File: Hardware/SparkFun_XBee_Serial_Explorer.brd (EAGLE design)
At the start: 57.1 x 48.3 mm, 45 parts, among them Q1 MBT2222, U1 MAX232SOIC16, U2 XBEE-1B3, U3 LM117

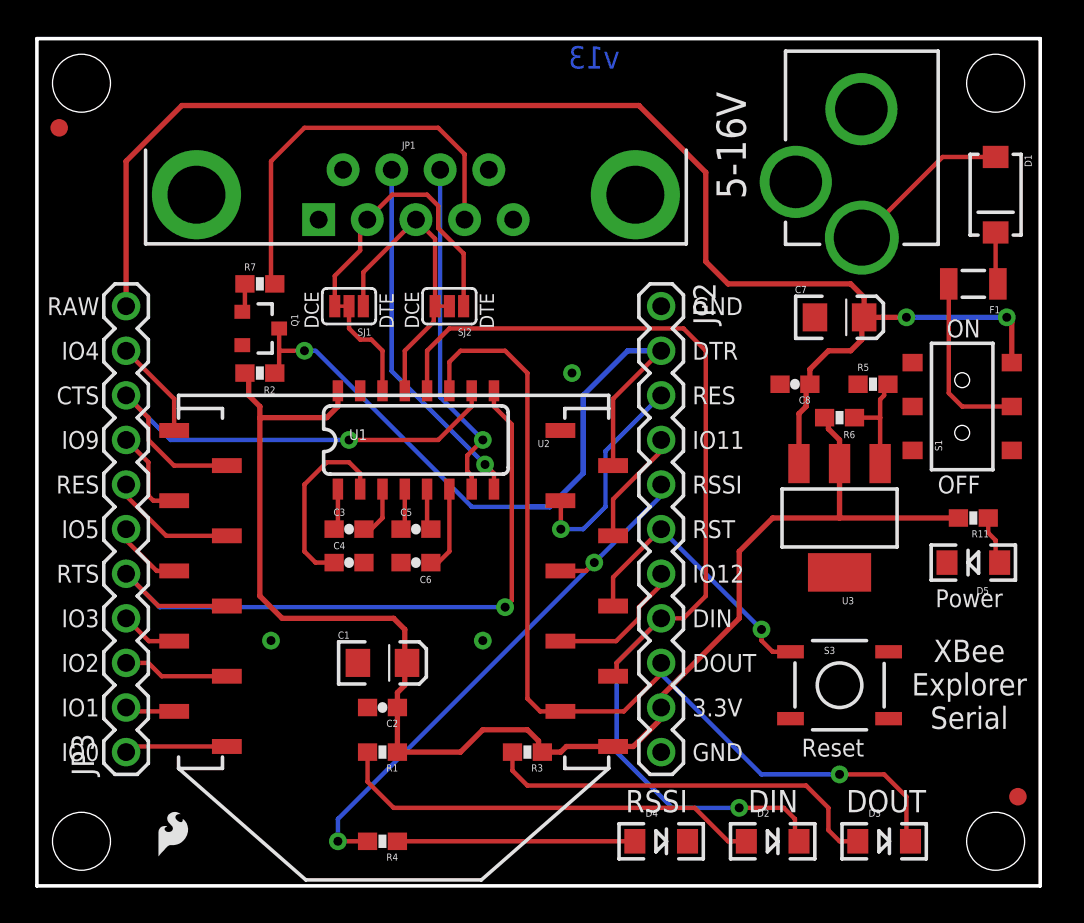
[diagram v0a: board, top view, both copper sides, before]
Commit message: Adding in test points for QC
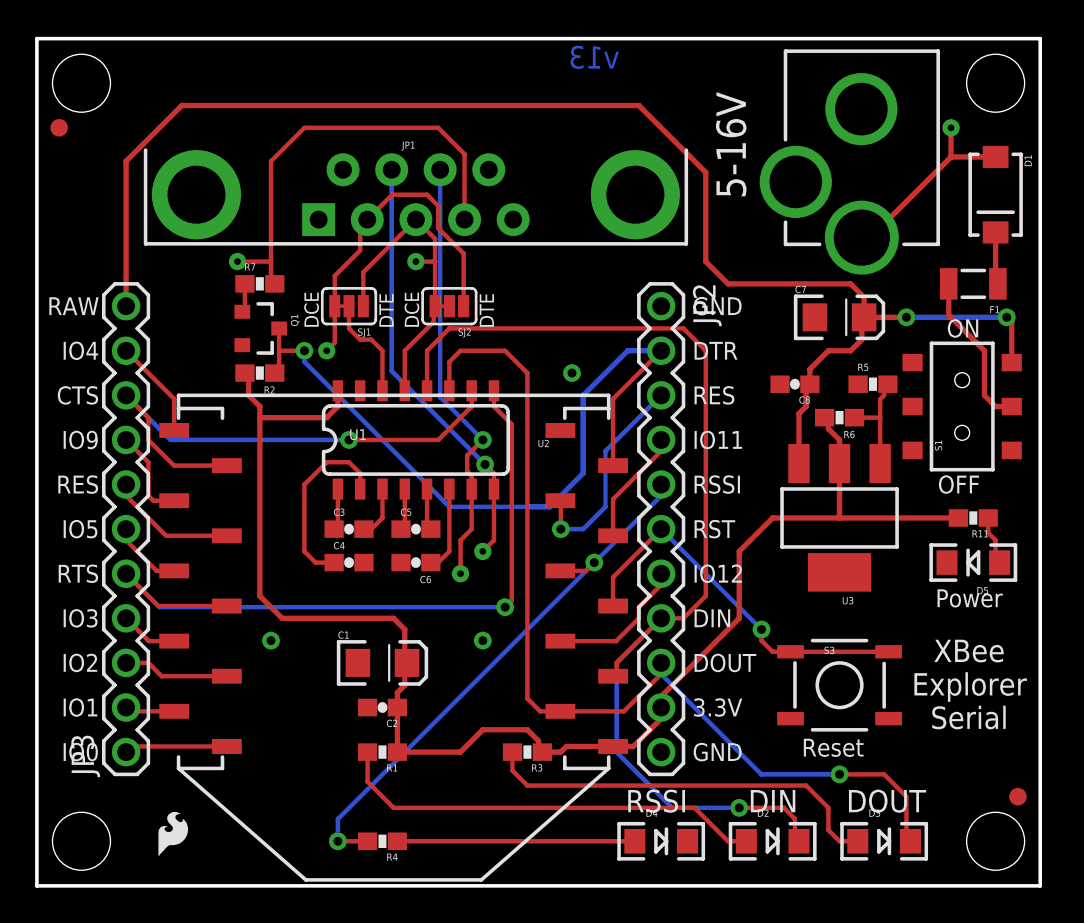
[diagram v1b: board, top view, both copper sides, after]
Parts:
- added TP1, TP2, TP3, TP4, TP5, TP6: TEST-POINTTP_15TH_THRU, SparkFun-Passives:TP_15TH
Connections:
- net N$15: now also TP6.P$1
- net RS232-CTS: now also TP2.P$1
- net RS232-DTR: now also TP3.P$1
- net RS232-RTS: now also TP1.P$1
- net RS232-RX: now also TP4.P$1
- net RS232-TX: now also TP5.P$1
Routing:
- net RESET: track 16.1 -> 22.1 mm
- net RS232-CTS: track 19.7 -> 24.8 mm
- net RS232-RTS: track 20.6 -> 24.4 mm
- net RS232-TX: track 16.9 -> 19.6 mm
- net RS232-DTR: track 23.2 -> 25.1 mm
- net N$15: track 9.52 -> 11.2 mm
- net N$11: track 10.1 -> 9.01 mm
- net RS232-RX: track 11.6 -> 12.6 mm
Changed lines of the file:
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@@
 <layer number="47" name="Measures" color="7" fill="1" visible="no" active="yes"/>
 <layer number="48" name="Document" color="7" fill="1" visible="no" active="yes"/>
-<layer number="49" name="Reference" color="7" fill="1" visible="no" active="yes"/>
+<layer number="49" name="Reference" color="7" fill="1" visible="yes" active="yes"/>
 <layer number="50" name="dxf" color="7" fill="1" visible="no" active="yes"/>
 <layer number="51" name="tDocu" color="6" fill="1" visible="yes" active="yes"/>
@@
 </element>
 <element name="LOGO3" library="SparkFun-Aesthetics" package="SFE_LOGO_FLAME_.1" value="SFE_LOGO_FLAME.1_INCH" x="6.604" y="1.3208"/>
+<element name="TP1" library="SparkFun-Passives" package="TP_15TH" value="TEST-POINTTP_15TH_THRU" x="25.4" y="19.05"/>
+<element name="TP2" library="SparkFun-Passives" package="TP_15TH" value="TEST-POINTTP_15TH_THRU" x="24.13" y="17.78"/>
+<element name="TP3" library="SparkFun-Passives" package="TP_15TH" value="TEST-POINTTP_15TH_THRU" x="11.43" y="35.56"/>
+<element name="TP4" library="SparkFun-Passives" package="TP_15TH" value="TEST-POINTTP_15TH_THRU" x="21.59" y="35.56"/>
+<element name="TP5" library="SparkFun-Passives" package="TP_15TH" value="TEST-POINTTP_15TH_THRU" x="16.51" y="30.48"/>
+<element name="TP6" library="SparkFun-Passives" package="TP_15TH" value="TEST-POINTTP_15TH_THRU" x="52.07" y="43.18"/>
 </elements>
 <signals>
@@
 <wire x1="32.82" y1="17.58" x2="35.56" y2="20.32" width="0.254" layer="1"/>
 <contactref element="S3" pad="2"/>
-<wire x1="42.926" y1="13.335" x2="48.514" y2="13.335" width="0" layer="19" extent="1-1"/>
+<wire x1="42.926" y1="13.335" x2="48.514" y2="13.335" width="0.254" layer="1"/>
+<wire x1="48.895" y1="13.335" x2="48.514" y2="13.335" width="0.254" layer="1"/>
 </signal>
 <signal name="RAW" class="1">
@@
 <contactref element="D1" pad="A"/>
 <contactref element="JP4" pad="PWR"/>
-<wire x1="54.61" y1="41.52" x2="51.5878" y2="41.52" width="0.254" layer="1"/>
-<wire x1="51.5878" y1="41.52" x2="46.99" y2="36.9222" width="0.254" layer="1"/>
+<contactref element="TP6" pad="P$1"/>
+<wire x1="52.07" y1="43.18" x2="52.07" y2="41.52" width="0.3048" layer="1"/>
+<wire x1="46.99" y1="36.9222" x2="47.4722" y2="36.9222" width="0.3048" layer="1"/>
+<wire x1="47.4722" y1="36.9222" x2="52.07" y2="41.52" width="0.3048" layer="1"/>
+<wire x1="52.07" y1="41.52" x2="54.61" y2="41.52" width="0.3048" layer="1"/>
 </signal>
 <signal name="N$16">
 <contactref element="D1" pad="C"/>
 <contactref element="F1" pad="1"/>
-<wire x1="54.61" y1="37.22" x2="54.61" y2="34.42" width="0.254" layer="1"/>
-<wire x1="54.61" y1="34.42" x2="54.74" y2="34.29" width="0.254" layer="1"/>
+<wire x1="54.61" y1="37.22" x2="54.61" y2="34.42" width="0.3048" layer="1"/>
+<wire x1="54.61" y1="34.42" x2="54.74" y2="34.29" width="0.3048" layer="1"/>
 </signal>
 <signal name="RS232-RTS">
@@
 <wire x1="20.21" y1="40.79" x2="20.21" y2="29.32" width="0.254" layer="16"/>
 <via x="25.527" y="24.003" extent="1-16" drill="0.508"/>
+<contactref element="TP1" pad="P$1"/>
+<wire x1="26.035" y1="22.6" x2="26.035" y2="19.685" width="0.254" layer="1"/>
+<wire x1="26.035" y1="19.685" x2="25.4" y2="19.05" width="0.254" layer="1"/>
 </signal>
 <signal name="RS232-CTS">
@@
 <wire x1="22.97" y1="27.83" x2="25.4" y2="25.4" width="0.254" layer="16"/>
 <via x="25.4" y="25.4" extent="1-16" drill="0.508"/>
+<contactref element="TP2" pad="P$1"/>
+<wire x1="24.765" y1="22.6" x2="24.765" y2="20.32" width="0.254" layer="1"/>
+<wire x1="24.765" y1="20.32" x2="24.13" y2="19.685" width="0.254" layer="1"/>
+<wire x1="24.13" y1="19.685" x2="24.13" y2="17.78" width="0.254" layer="1"/>
 </signal>
 <signal name="RS232-DTR">
@@
 <wire x1="15.24" y1="43.18" x2="22.86" y2="43.18" width="0.254" layer="1"/>
 <wire x1="13.335" y1="41.275" x2="15.24" y2="43.18" width="0.254" layer="1"/>
-<wire x1="13.335" y1="41.275" x2="13.335" y2="34.505" width="0.254" layer="1"/>
+<wire x1="13.335" y1="41.275" x2="13.335" y2="35.56" width="0.254" layer="1"/>
+<wire x1="13.335" y1="35.56" x2="13.335" y2="34.505" width="0.254" layer="1"/>
 <wire x1="13.335" y1="34.505" x2="13.55" y2="34.29" width="0.254" layer="1"/>
+<contactref element="TP3" pad="P$1"/>
+<wire x1="11.43" y1="35.56" x2="13.335" y2="35.56" width="0.254" layer="1"/>
 </signal>
 <signal name="RS232-RX">
@@
 <wire x1="18.5928" y1="33.02" x2="18.5928" y2="34.9528" width="0.254" layer="1"/>
 <wire x1="18.5928" y1="34.9528" x2="21.59" y2="37.95" width="0.254" layer="1"/>
-<wire x1="22.6822" y1="33.02" x2="22.6822" y2="36.8578" width="0.254" layer="1"/>
+<wire x1="22.6822" y1="33.02" x2="22.6822" y2="35.56" width="0.254" layer="1"/>
+<wire x1="22.6822" y1="35.56" x2="22.6822" y2="36.8578" width="0.254" layer="1"/>
 <wire x1="22.6822" y1="36.8578" x2="21.59" y2="37.95" width="0.254" layer="1"/>
+<contactref element="TP4" pad="P$1"/>
+<wire x1="21.59" y1="35.56" x2="22.6822" y2="35.56" width="0.254" layer="1"/>
 </signal>
 <signal name="DTR">
@@
 <contactref element="U2" pad="9"/>
 <contactref element="JP2" pad="2"/>
-<wire x1="24.765" y1="21.59" x2="27.94" y2="21.59" width="0.254" layer="16"/>
+<wire x1="23.495" y1="21.59" x2="27.94" y2="21.59" width="0.254" layer="16"/>
 <via x="15.24" y="30.48" extent="1-16" drill="0.508"/>
 <wire x1="32.82" y1="23.94" x2="32.82" y2="27.74" width="0.254" layer="1"/>
@@
 <wire x1="13.8" y1="29.46" x2="13.55" y2="29.21" width="0.254" layer="1"/>
 <wire x1="15.24" y1="30.48" x2="13.8" y2="30.48" width="0.254" layer="1"/>
-<wire x1="24.765" y1="21.59" x2="15.875" y2="30.48" width="0.254" layer="16"/>
-<wire x1="15.875" y1="30.48" x2="15.24" y2="30.48" width="0.254" layer="16"/>
 <wire x1="27.94" y1="21.59" x2="29.21" y2="21.59" width="0.3048" layer="16"/>
 <wire x1="29.21" y1="21.59" x2="31.115" y2="23.495" width="0.3048" layer="16"/>
@@
 <wire x1="31.115" y1="27.94" x2="33.655" y2="30.48" width="0.3048" layer="16"/>
 <wire x1="33.655" y1="30.48" x2="35.56" y2="30.48" width="0.3048" layer="16"/>
+<wire x1="23.495" y1="21.59" x2="15.24" y2="29.845" width="0.254" layer="16"/>
+<wire x1="15.24" y1="29.845" x2="15.24" y2="30.48" width="0.254" layer="16"/>
 </signal>
 <signal name="N$10">
@@
 <contactref element="F1" pad="2"/>
 <contactref element="S1" pad="5"/>
-<wire x1="51.94" y1="34.29" x2="51.94" y2="28.07" width="0.254" layer="1"/>
-<wire x1="51.94" y1="28.07" x2="52.705" y2="27.305" width="0.254" layer="1"/>
-<wire x1="52.705" y1="27.305" x2="55.53" y2="27.305" width="0.254" layer="1"/>
+<wire x1="51.94" y1="34.29" x2="51.94" y2="32.515" width="0.3048" layer="1"/>
+<wire x1="51.94" y1="32.515" x2="53.975" y2="30.48" width="0.3048" layer="1"/>
+<wire x1="53.975" y1="30.48" x2="53.975" y2="27.94" width="0.3048" layer="1"/>
+<wire x1="53.975" y1="27.94" x2="54.61" y2="27.305" width="0.3048" layer="1"/>
+<wire x1="54.61" y1="27.305" x2="55.53" y2="27.305" width="0.3048" layer="1"/>
 </signal>
 <signal name="N$12">
@@
 <wire x1="22.86" y1="37.465" x2="24.3078" y2="36.0172" width="0.254" layer="1"/>
 <wire x1="24.3078" y1="33.02" x2="24.3078" y2="36.0172" width="0.254" layer="1"/>
+<contactref element="TP5" pad="P$1"/>
+<wire x1="16.9672" y1="33.02" x2="16.9672" y2="30.9372" width="0.254" layer="1"/>
+<wire x1="16.9672" y1="30.9372" x2="16.51" y2="30.48" width="0.254" layer="1"/>
 </signal>
 </signals>

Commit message: Fixing PTC part number for proper BOM
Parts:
- F1: value PTCSMD -> PTCTHERMISTOR1206
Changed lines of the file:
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@@
 <setting verticaltext="up"/>
 </settings>
-<grid distance="0.025" unitdist="inch" unit="inch" style="lines" multiple="1" display="yes" altdistance="0.005" altunitdist="inch" altunit="inch"/>
+<grid distance="0.05" unitdist="inch" unit="inch" style="lines" multiple="1" display="yes" altdistance="0.005" altunitdist="inch" altunit="inch"/>
 <layers>
 <layer number="1" name="Top" color="4" fill="1" visible="yes" active="yes"/>
@@
 <layer number="47" name="Measures" color="7" fill="1" visible="no" active="yes"/>
 <layer number="48" name="Document" color="7" fill="1" visible="no" active="yes"/>
-<layer number="49" name="Reference" color="7" fill="1" visible="yes" active="yes"/>
+<layer number="49" name="Reference" color="7" fill="1" visible="no" active="yes"/>
 <layer number="50" name="dxf" color="7" fill="1" visible="no" active="yes"/>
 <layer number="51" name="tDocu" color="6" fill="1" visible="yes" active="yes"/>
@@
 <attribute name="PROD_ID" value="CAP-00810" x="43.18" y="28.575" size="1.778" layer="27" rot="R180" display="off"/>
 </element>
-<element name="F1" library="SparkFun-PowerIC" package="PTC-1206" value="PTCSMD" x="53.34" y="34.29" smashed="yes" rot="R180">
+<element name="F1" library="SparkFun-PowerIC" package="PTC-1206" value="PTCTHERMISTOR1206" x="53.34" y="34.29" smashed="yes" rot="R180">
 <attribute name="NAME" x="54.864" y="33.02" size="0.4064" layer="25" rot="R180"/>
 <attribute name="VALUE" x="54.864" y="35.941" size="0.4064" layer="27" rot="R180"/>
-<attribute name="PROD_ID" value="RES-11150" x="53.34" y="34.29" size="1.778" layer="27" rot="R180" display="off"/>
+<attribute name="PROD_ID" value="RES-08585" x="53.34" y="34.29" size="1.778" layer="27" rot="R180" display="off"/>
 </element>
 <element name="Q1" library="SparkFun-DiscreteSemi" package="SOT23-3" value="MBT2222" x="12.7" y="31.75" rot="R270">

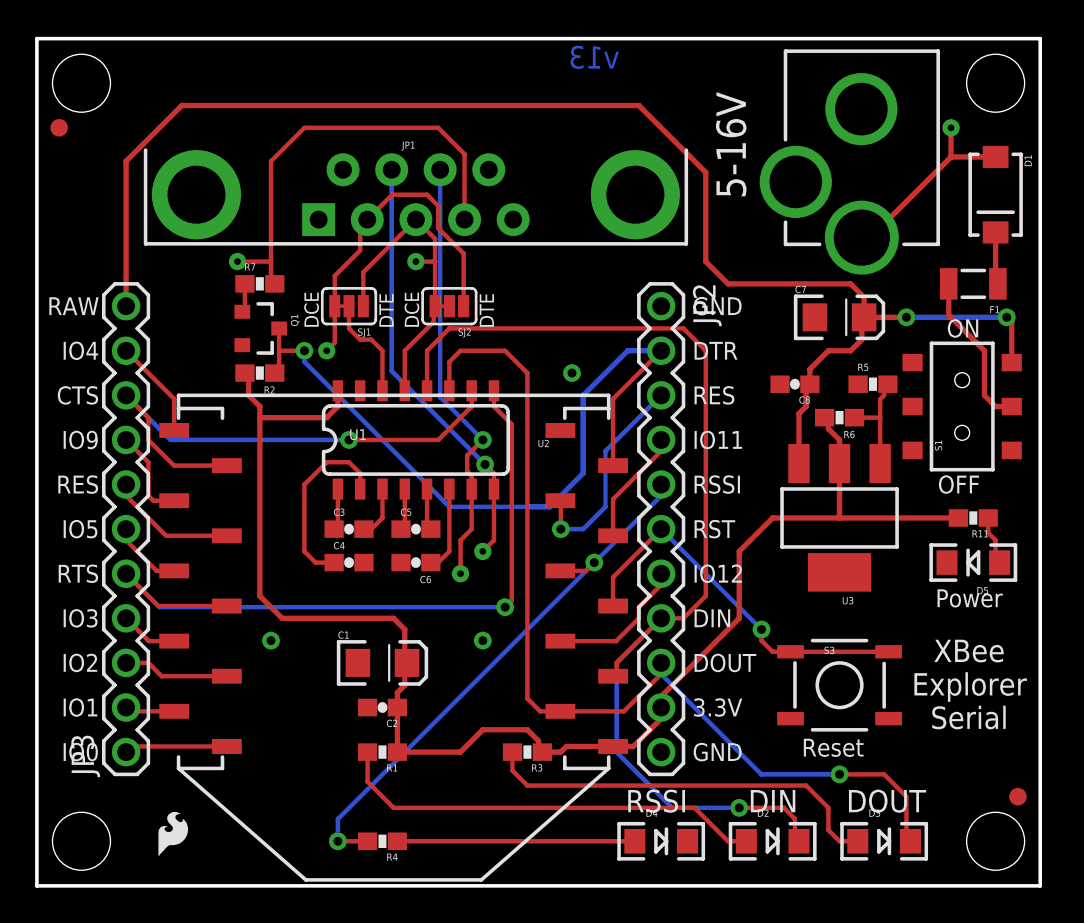
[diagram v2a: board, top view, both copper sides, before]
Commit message: Moving test points away from selective solder points/moving board name
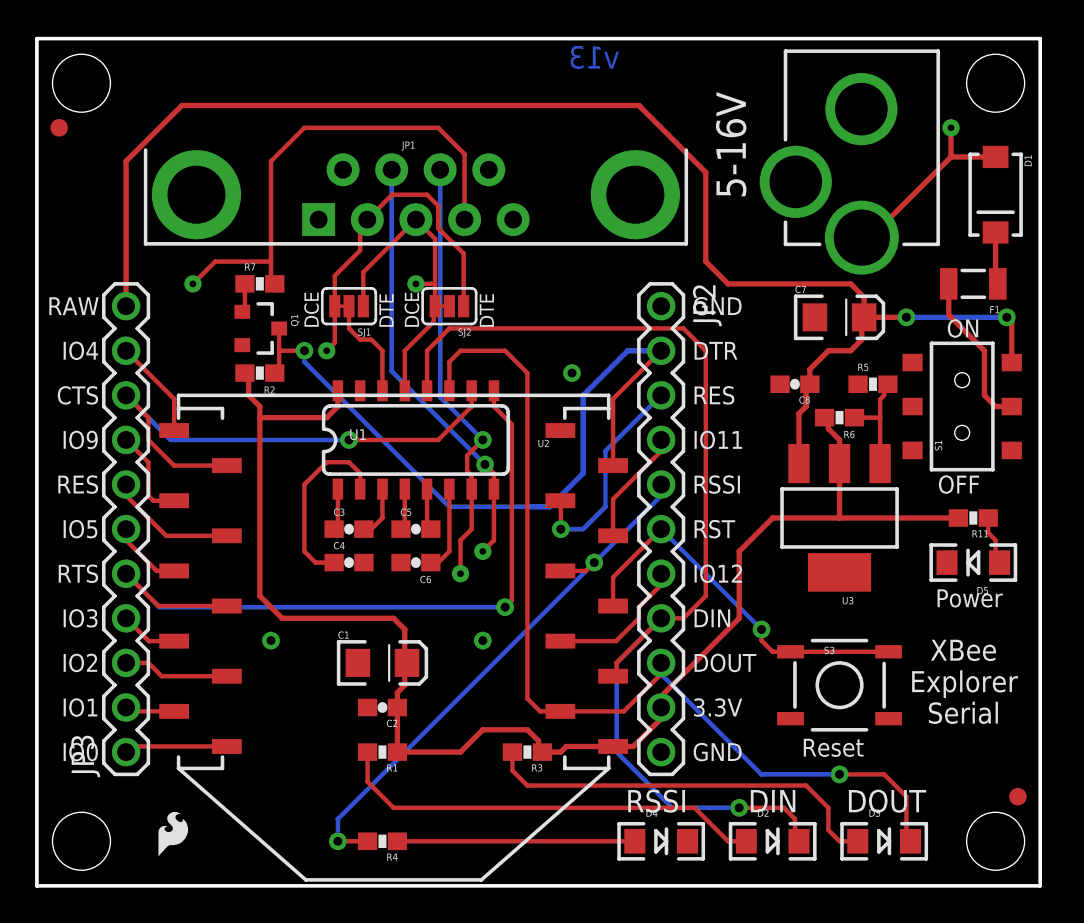
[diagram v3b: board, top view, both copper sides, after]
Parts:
- moved TP3 2.84 mm to (8.89, 34.3)
- moved TP4 1.27 mm to (21.6, 34.3)
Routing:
- net RS232-DTR: track 25.1 -> 28.2 mm
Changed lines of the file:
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@@
 <?xml version="1.0" encoding="utf-8"?>
 <!DOCTYPE eagle SYSTEM "eagle.dtd">
-<eagle version="7.1.0">
+<eagle version="7.2.0">
 <drawing>
 <settings>
@@
 <layer number="47" name="Measures" color="7" fill="1" visible="no" active="yes"/>
 <layer number="48" name="Document" color="7" fill="1" visible="no" active="yes"/>
-<layer number="49" name="Reference" color="7" fill="1" visible="no" active="yes"/>
+<layer number="49" name="Reference" color="7" fill="1" visible="yes" active="yes"/>
 <layer number="50" name="dxf" color="7" fill="1" visible="no" active="yes"/>
 <layer number="51" name="tDocu" color="6" fill="1" visible="yes" active="yes"/>
@@
 <dimension x1="5.08" y1="7.62" x2="5.08" y2="33.02" x3="-14.5288" y3="20.32" textsize="1.4224" textratio="15" layer="47" visible="yes"/>
 <dimension x1="2.54" y1="2.54" x2="54.1528" y2="2.6416" x3="28.3568" y3="-2.692378125" textsize="1.4224" textratio="15" layer="47" visible="yes"/>
-<text x="53.1114" y="14.0208" size="1.27" layer="21" font="vector" ratio="15" rot="R180" align="bottom-center">XBee
+<text x="52.7939" y="14.0208" size="1.1938" layer="21" font="vector" ratio="15" rot="R180" align="bottom-center">XBee
 Explorer
 Serial
@@
 <element name="TP1" library="SparkFun-Passives" package="TP_15TH" value="TEST-POINTTP_15TH_THRU" x="25.4" y="19.05"/>
 <element name="TP2" library="SparkFun-Passives" package="TP_15TH" value="TEST-POINTTP_15TH_THRU" x="24.13" y="17.78"/>
-<element name="TP3" library="SparkFun-Passives" package="TP_15TH" value="TEST-POINTTP_15TH_THRU" x="11.43" y="35.56"/>
-<element name="TP4" library="SparkFun-Passives" package="TP_15TH" value="TEST-POINTTP_15TH_THRU" x="21.59" y="35.56"/>
+<element name="TP3" library="SparkFun-Passives" package="TP_15TH" value="TEST-POINTTP_15TH_THRU" x="8.89" y="34.29"/>
+<element name="TP4" library="SparkFun-Passives" package="TP_15TH" value="TEST-POINTTP_15TH_THRU" x="21.59" y="34.29"/>
 <element name="TP5" library="SparkFun-Passives" package="TP_15TH" value="TEST-POINTTP_15TH_THRU" x="16.51" y="30.48"/>
 <element name="TP6" library="SparkFun-Passives" package="TP_15TH" value="TEST-POINTTP_15TH_THRU" x="52.07" y="43.18"/>
@@
 <wire x1="13.335" y1="34.505" x2="13.55" y2="34.29" width="0.254" layer="1"/>
 <contactref element="TP3" pad="P$1"/>
-<wire x1="11.43" y1="35.56" x2="13.335" y2="35.56" width="0.254" layer="1"/>
+<wire x1="8.89" y1="34.29" x2="10.16" y2="35.56" width="0.254" layer="1"/>
+<wire x1="10.16" y1="35.56" x2="13.335" y2="35.56" width="0.254" layer="1"/>
 </signal>
 <signal name="RS232-RX">
@@
 <wire x1="18.5928" y1="33.02" x2="18.5928" y2="34.9528" width="0.254" layer="1"/>
 <wire x1="18.5928" y1="34.9528" x2="21.59" y2="37.95" width="0.254" layer="1"/>
-<wire x1="22.6822" y1="33.02" x2="22.6822" y2="35.56" width="0.254" layer="1"/>
-<wire x1="22.6822" y1="35.56" x2="22.6822" y2="36.8578" width="0.254" layer="1"/>
+<wire x1="22.6822" y1="33.02" x2="22.6822" y2="34.29" width="0.254" layer="1"/>
+<wire x1="22.6822" y1="34.29" x2="22.6822" y2="36.8578" width="0.254" layer="1"/>
 <wire x1="22.6822" y1="36.8578" x2="21.59" y2="37.95" width="0.254" layer="1"/>
 <contactref element="TP4" pad="P$1"/>
-<wire x1="21.59" y1="35.56" x2="22.6822" y2="35.56" width="0.254" layer="1"/>
+<wire x1="21.59" y1="34.29" x2="22.6822" y2="34.29" width="0.254" layer="1"/>
 </signal>
 <signal name="DTR">
